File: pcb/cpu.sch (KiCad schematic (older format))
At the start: 34 parts, among them P27 BDM, P57 TX1, P58 RX1, P59 RX0-TX0, P64 CAN-RX-TX, U1 MC9S12XDP512, Y1 16MHz

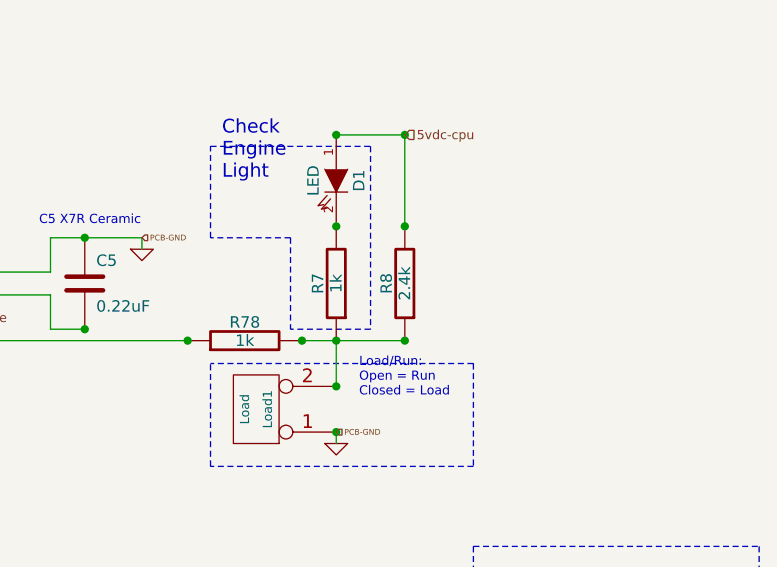
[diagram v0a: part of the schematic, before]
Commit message: Changed 2.4k ohm resistor to 2.43k ohm resistor due to physical size issue.
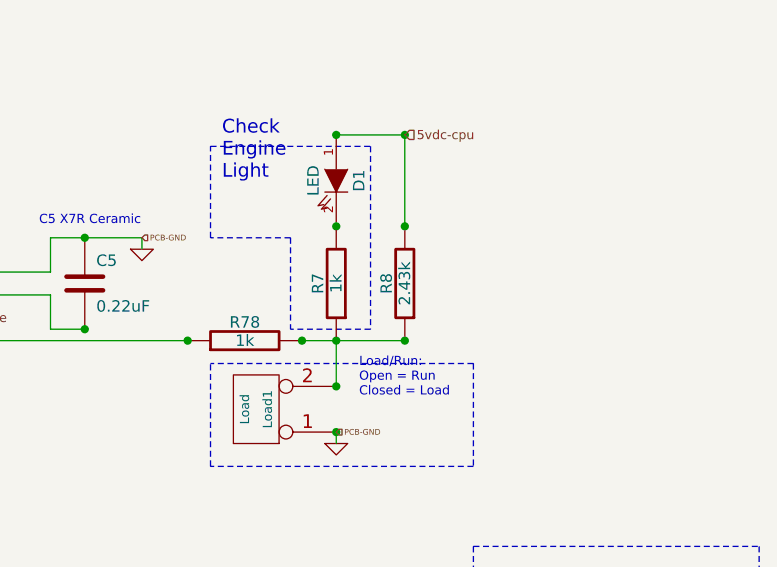
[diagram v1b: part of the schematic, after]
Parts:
- R8: value 2.4k -> 2.43k
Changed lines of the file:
@@
-EESchema Schematic File Version 2  date Wed 18 Sep 2013 09:15:01 PM EDT
+EESchema Schematic File Version 2
 LIBS:opto
 LIBS:power
@@
 LIBS:Jaguar
 LIBS:Jaguar-cache
-EELAYER 24  0
+EELAYER 27 0
 EELAYER END
-$Descr A4 11700 8267
+$Descr A4 11693 8268
+encoding utf-8
 Sheet 2 7
 Title "Jaguar PCB for FreeEMS"
-Date "16 sep 2013"
+Date "7 nov 2013"
 Rev "0.6-alpha"
 Comp "Git: 73f4fbd6d6"
@@
 F 0 "P59" V 5750 800 40  0000 C CNN
 F 1 "RX0-TX0" V 5850 800 40  0000 C CNN
+F 2 "" H 5800 800 60  0001 C CNN
+F 3 "" H 5800 800 60  0001 C CNN
 	1    5800 800
 	0    -1   -1   0
@@
 F 0 "P64" V 4050 1300 40  0000 C CNN
 F 1 "CAN-RX-TX" V 4150 1300 40  0000 C CNN
+F 2 "" H 4100 1300 60  0001 C CNN
+F 3 "" H 4100 1300 60  0001 C CNN
 	1    4100 1300
 	0    -1   -1   0
@@
 F 0 "P57" H 5380 1600 40  0000 L CNN
 F 1 "TX1" H 5300 1655 30  0001 C CNN
+F 2 "" H 5300 1600 60  0001 C CNN
+F 3 "" H 5300 1600 60  0001 C CNN
 	1    5300 1600
 	0    -1   -1   0
@@
 F 0 "P58" H 5480 1600 40  0000 L CNN
 F 1 "RX1" H 5400 1655 30  0001 C CNN
+F 2 "" H 5400 1600 60  0001 C CNN
+F 3 "" H 5400 1600 60  0001 C CNN
 	1    5400 1600
 	0    -1   -1   0
@@
 F 0 "C47" H 3700 400 50  0000 L CNN
 F 1 "10uF" H 3700 250 50  0000 L CNN
+F 2 "" H 3850 550 60  0001 C CNN
+F 3 "" H 3850 550 60  0001 C CNN
 	1    3850 550
 	0    -1   -1   0
@@
 F 0 "R78" V 8630 4850 50  0000 C CNN
 F 1 "1k" V 8550 4850 50  0000 C CNN
+F 2 "" H 8550 4850 60  0001 C CNN
+F 3 "" H 8550 4850 60  0001 C CNN
 	1    8550 4850
 	0    -1   -1   0
@@
 F 0 "PP2" V 3400 1400 50  0000 C CNN
 F 1 "Port P4-7" V 3500 1400 50  0000 C CNN
+F 2 "" H 3450 1400 60  0001 C CNN
+F 3 "" H 3450 1400 60  0001 C CNN
 	1    3450 1400
 	0    -1   -1   0
@@
 F 0 "PP1" V 1800 3000 50  0000 C CNN
 F 1 "Port P0-3" V 1900 3000 50  0000 C CNN
+F 2 "" H 1850 3000 60  0001 C CNN
+F 3 "" H 1850 3000 60  0001 C CNN
 	1    1850 3000
 	-1   0    0    1
@@
 F 0 "C48" H 4650 7650 50  0000 L CNN
 F 1 "10uF" H 4650 7450 50  0000 L CNN
+F 2 "" H 4600 7550 60  0001 C CNN
+F 3 "" H 4600 7550 60  0001 C CNN
 	1    4600 7550
 	0    1    1    0
@@
 F 0 "C5" H 7900 4700 50  0000 L CNN
 F 1 "0.22uF" H 7900 4500 50  0000 L CNN
+F 2 "" H 7850 4600 60  0001 C CNN
+F 3 "" H 7850 4600 60  0001 C CNN
 	1    7850 4600
 	1    0    0    -1
@@
 F 0 "C1" H 1350 4200 50  0000 L CNN
 F 1 "0.22uF" H 1350 4000 50  0000 L CNN
+F 2 "" H 1300 4100 60  0001 C CNN
+F 3 "" H 1300 4100 60  0001 C CNN
 	1    1300 4100
 	-1   0    0    1
@@
 F 0 "Load1" V 8550 5150 40  0000 C CNN
 F 1 "Load" V 8650 5150 40  0000 C CNN
+F 2 "" H 8600 5150 60  0001 C CNN
+F 3 "" H 8600 5150 60  0001 C CNN
 	1    8600 5150
 	-1   0    0    1
@@
 F 0 "#PWR02" H 1300 4350 30  0001 C CNN
 F 1 "GND" H 1300 4280 30  0001 C CNN
+F 2 "" H 1300 4350 60  0001 C CNN
+F 3 "" H 1300 4350 60  0001 C CNN
 	1    1300 4350
 	1    0    0    -1
@@
 F 0 "C44" H 7200 2050 50  0000 L CNN
 F 1 "0.22uF" H 7200 1850 50  0000 L CNN
+F 2 "" H 7150 1950 60  0001 C CNN
+F 3 "" H 7150 1950 60  0001 C CNN
 	1    7150 1950
 	1    0    0    -1
@@
 F 0 "#PWR03" H 5200 6850 30  0001 C CNN
 F 1 "GND" H 5200 6780 30  0001 C CNN
+F 2 "" H 5200 6850 60  0001 C CNN
+F 3 "" H 5200 6850 60  0001 C CNN
 	1    5200 6850
 	1    0    0    -1
@@
 F 0 "#PWR04" H 8450 6000 30  0001 C CNN
 F 1 "GND" H 8450 5930 30  0001 C CNN
+F 2 "" H 8450 6000 60  0001 C CNN
+F 3 "" H 8450 6000 60  0001 C CNN
 	1    8450 6000
 	1    0    0    -1
@@
 F 0 "#PWR05" H 1700 7000 30  0001 C CNN
 F 1 "GND" H 1700 6930 30  0001 C CNN
+F 2 "" H 1700 7000 60  0001 C CNN
+F 3 "" H 1700 7000 60  0001 C CNN
 	1    1700 7000
 	1    0    0    -1
@@
 F 0 "#PWR06" H 1850 7600 30  0001 C CNN
 F 1 "GND" H 1850 7530 30  0001 C CNN
+F 2 "" H 1850 7600 60  0001 C CNN
+F 3 "" H 1850 7600 60  0001 C CNN
 	1    1850 7600
 	1    0    0    -1
@@
 F 0 "#PWR07" H 4300 1100 30  0001 C CNN
 F 1 "GND" H 4300 1030 30  0001 C CNN
+F 2 "" H 4300 1100 60  0001 C CNN
+F 3 "" H 4300 1100 60  0001 C CNN
 	1    4300 1100
 	1    0    0    -1
@@
 F 0 "#PWR08" H 8950 1000 30  0001 C CNN
 F 1 "GND" H 8950 930 30  0001 C CNN
+F 2 "" H 8950 1000 60  0001 C CNN
+F 3 "" H 8950 1000 60  0001 C CNN
 	1    8950 1000
 	1    0    0    -1
@@
 F 0 "#PWR09" H 6100 1850 30  0001 C CNN
 F 1 "GND" H 6100 1780 30  0001 C CNN
+F 2 "" H 6100 1850 60  0001 C CNN
+F 3 "" H 6100 1850 60  0001 C CNN
 	1    6100 1850
 	1    0    0    -1
@@
 F 0 "#PWR010" H 8950 5300 30  0001 C CNN
 F 1 "GND" H 8950 5230 30  0001 C CNN
+F 2 "" H 8950 5300 60  0001 C CNN
+F 3 "" H 8950 5300 60  0001 C CNN
 	1    8950 5300
 	1    0    0    -1
@@
 F 0 "#PWR011" H 8100 4450 30  0001 C CNN
 F 1 "GND" H 8100 4380 30  0001 C CNN
+F 2 "" H 8100 4450 60  0001 C CNN
+F 3 "" H 8100 4450 60  0001 C CNN
 	1    8100 4450
 	1    0    0    -1
@@
 F 0 "#PWR012" H 9950 6850 30  0001 C CNN
 F 1 "GND" H 9950 6780 30  0001 C CNN
+F 2 "" H 9950 6850 60  0001 C CNN
+F 3 "" H 9950 6850 60  0001 C CNN
 	1    9950 6850
 	1    0    0    -1
@@
 F 0 "#PWR013" H 4400 7700 30  0001 C CNN
 F 1 "GND" H 4400 7630 30  0001 C CNN
+F 2 "" H 4400 7700 60  0001 C CNN
+F 3 "" H 4400 7700 60  0001 C CNN
 	1    4400 7700
 	1    0    0    -1
@@
 F 0 "#PWR014" H 4100 7700 30  0001 C CNN
 F 1 "GND" H 4100 7630 30  0001 C CNN
+F 2 "" H 4100 7700 60  0001 C CNN
+F 3 "" H 4100 7700 60  0001 C CNN
 	1    4100 7700
 	1    0    0    -1
@@
 F 0 "D1" H 8950 4250 50  0000 C CNN
 F 1 "LED" H 8950 4050 50  0000 C CNN
+F 2 "" H 8950 4150 60  0001 C CNN
+F 3 "" H 8950 4150 60  0001 C CNN
 	1    8950 4150
 	0    1    1    0
@@
 P 9250 4600
 F 0 "R8" V 9330 4600 50  0000 C CNN
-F 1 "2.4k" V 9250 4600 50  0000 C CNN
+F 1 "2.43k" V 9250 4600 50  0000 C CNN
+F 2 "" H 9250 4600 60  0001 C CNN
+F 3 "" H 9250 4600 60  0001 C CNN
 	1    9250 4600
 	-1   0    0    1
@@
 F 0 "C6" H 1900 7450 50  0000 L CNN
 F 1 "0.1uF" H 1900 7250 50  0000 L CNN
+F 2 "" H 1850 7350 60  0001 C CNN
+F 3 "" H 1850 7350 60  0001 C CNN
 	1    1850 7350
 	1    0    0    -1
@@
 F 1 "MC9S12XDP512" H 4300 3750 50  0000 L BNN
 F 2 "mc9s12xdp512-LQFP112" H 4600 4300 50  0001 C CNN
+F 3 "" H 4600 4150 60  0001 C CNN
 	1    4600 4150
 	1    0    0    -1
@@
 F 0 "P27" H 1200 7450 50  0000 C CNN
 F 1 "BDM" V 1200 7250 40  0000 C CNN
+F 2 "" H 1200 7200 60  0001 C CNN
+F 3 "" H 1200 7200 60  0001 C CNN
 	1    1200 7200
 	1    0    0    -1
@@
 F 0 "R4" V 880 6800 50  0000 C CNN
 F 1 "10k" V 800 6800 50  0000 C CNN
+F 2 "" H 800 6800 60  0001 C CNN
+F 3 "" H 800 6800 60  0001 C CNN
 	1    800  6800
 	-1   0    0    1
@@
 F 0 "R5" V 1930 6800 50  0000 C CNN
 F 1 "10k" V 1850 6800 50  0000 C CNN
+F 2 "" H 1850 6800 60  0001 C CNN
+F 3 "" H 1850 6800 60  0001 C CNN
 	1    1850 6800
 	-1   0    0    1
@@
 F 0 "R1" V 3700 7250 50  0000 C CNN
 F 1 "10k" V 3800 7250 50  0000 C CNN
+F 2 "" H 3800 7250 60  0001 C CNN
+F 3 "" H 3800 7250 60  0001 C CNN
 	1    3800 7250
 	1    0    0    -1
@@
 F 0 "R2" V 3900 7250 50  0000 C CNN
 F 1 "10k" V 4000 7250 50  0000 C CNN
+F 2 "" H 4000 7250 60  0001 C CNN
+F 3 "" H 4000 7250 60  0001 C CNN
 	1    4000 7250
 	1    0    0    -1
@@
 F 0 "R3" V 4100 7250 50  0000 C CNN
 F 1 "10k" V 4200 7250 50  0000 C CNN
+F 2 "" H 4200 7250 60  0001 C CNN
+F 3 "" H 4200 7250 60  0001 C CNN
 	1    4200 7250
 	1    0    0    -1
@@
 F 0 "R7" V 9030 4600 50  0000 C CNN
 F 1 "1k" V 8950 4600 50  0000 C CNN
+F 2 "" H 8950 4600 60  0001 C CNN
+F 3 "" H 8950 4600 60  0001 C CNN
 	1    8950 4600
 	-1   0    0    1
@@
 F 0 "Y1" H 10400 6000 60  0000 C CNN
 F 1 "16MHz" H 10200 5800 60  0000 C CNN
+F 2 "" H 10200 5950 60  0001 C CNN
+F 3 "" H 10200 5950 60  0001 C CNN
 	1    10200 5950
 	1    0    0    -1
@@
 F 0 "C11" H 10500 6700 50  0000 L CNN
 F 1 "20pF" H 10500 6500 50  0000 L CNN
+F 2 "" H 10450 6600 60  0001 C CNN
+F 3 "" H 10450 6600 60  0001 C CNN
 	1    10450 6600
 	-1   0    0    1
@@
 F 0 "C10" H 10000 6700 50  0000 L CNN
 F 1 "20pF" H 10000 6500 50  0000 L CNN
+F 2 "" H 9950 6600 60  0001 C CNN
+F 3 "" H 9950 6600 60  0001 C CNN
 	1    9950 6600
 	-1   0    0    1
@@
 F 0 "R6" V 8230 6750 50  0000 C CNN
 F 1 "3.3k" V 8150 6750 50  0000 C CNN
+F 2 "" H 8150 6750 60  0001 C CNN
+F 3 "" H 8150 6750 60  0001 C CNN
 	1    8150 6750
 	0    -1   -1   0
@@
 F 0 "C9" H 8450 6650 50  0000 L CNN
 F 1 "680pF" H 8450 6450 50  0000 L CNN
+F 2 "" H 8400 6550 60  0001 C CNN
+F 3 "" H 8400 6550 60  0001 C CNN
 	1    8400 6550
 	-1   0    0    1
@@
 F 0 "C7" H 7950 6650 50  0000 L CNN
 F 1 "6.8nF" H 7950 6450 50  0000 L CNN
+F 2 "" H 7900 6550 60  0001 C CNN
+F 3 "" H 7900 6550 60  0001 C CNN
 	1    7900 6550
 	-1   0    0    1
@@
 F 0 "C8" H 8200 6250 50  0000 L CNN
 F 1 "0.22uF" H 8200 6050 50  0000 L CNN
+F 2 "" H 8150 6150 60  0001 C CNN
+F 3 "" H 8150 6150 60  0001 C CNN
 	1    8150 6150
 	1    0    0    -1
@@
 F 0 "C3" H 4650 7400 50  0000 L CNN
 F 1 "0.22uF" H 4650 7200 50  0000 L CNN
+F 2 "" H 4600 7300 60  0001 C CNN
+F 3 "" H 4600 7300 60  0001 C CNN
 	1    4600 7300
 	0    -1   -1   0
@@
 F 0 "C4" H 5950 1650 50  0000 L CNN
 F 1 "0.22uF" H 6050 1550 50  0000 L CNN
+F 2 "" H 5900 1550 60  0001 C CNN
+F 3 "" H 5900 1550 60  0001 C CNN
 	1    5900 1550
 	1    0    0    -1
@@
 F 0 "C2" H 3900 1000 50  0000 L CNN
 F 1 "0.22uF" H 3750 600 50  0000 L CNN
+F 2 "" H 3850 900 60  0001 C CNN
+F 3 "" H 3850 900 60  0001 C CNN
 	1    3850 900
 	0    -1   -1   0

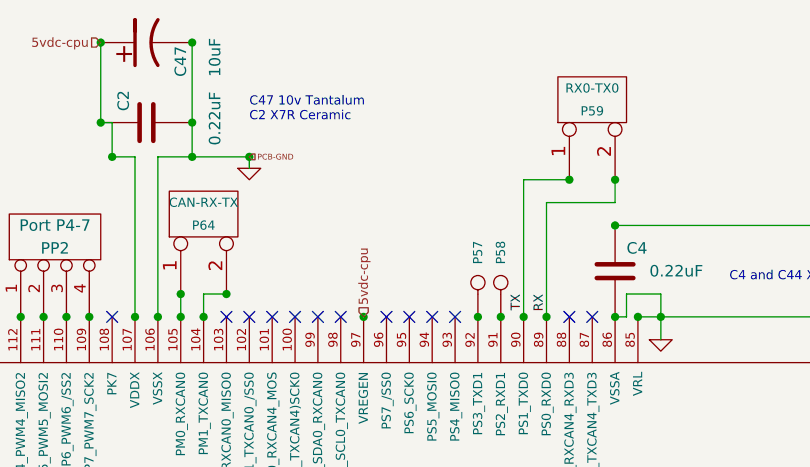
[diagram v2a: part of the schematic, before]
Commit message: Eliminated Pxx designations on the wire connection points and replaced them with the PCB silkscreen designations.
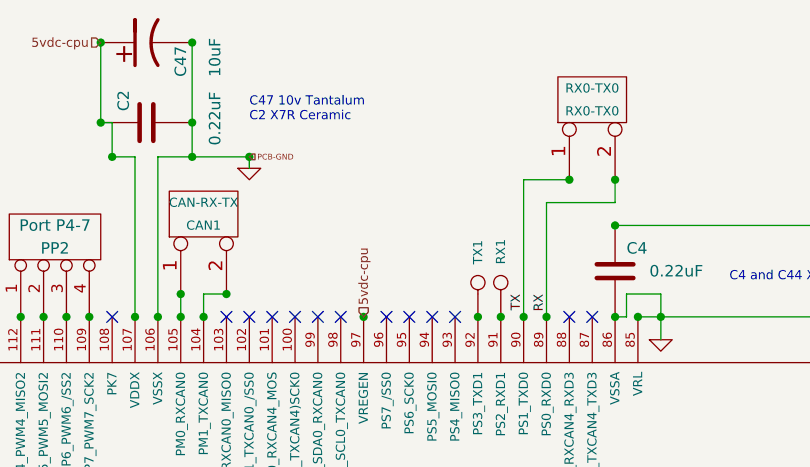
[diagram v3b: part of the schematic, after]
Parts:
- renumbered P64 to CAN1, P59 to RX0-TX0, P58 to RX1, P57 to TX1
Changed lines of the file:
@@
 Sheet 2 7
 Title "Jaguar PCB for FreeEMS"
-Date "17 nov 2013"
+Date "3 dec 2013"
 Rev "0.6-alpha"
 Comp "Git: 73f4fbd6d6"
@@
 	5900 1250 5900 1150
 $Comp
-L CONN_2 P59
+L CONN_2 RX0-TX0
 U 1 1 51A0194D
 P 5800 800
-F 0 "P59" V 5750 800 40  0000 C CNN
+F 0 "RX0-TX0" V 5750 800 40  0000 C CNN
 F 1 "RX0-TX0" V 5850 800 40  0000 C CNN
 F 2 "" H 5800 800 60  0001 C CNN
@@
 $EndComp
 $Comp
-L CONN_2 P64
+L CONN_2 CAN1
 U 1 1 519BDE3D
 P 4100 1300
-F 0 "P64" V 4050 1300 40  0000 C CNN
+F 0 "CAN1" V 4050 1300 40  0000 C CNN
 F 1 "CAN-RX-TX" V 4150 1300 40  0000 C CNN
 F 2 "" H 4100 1300 60  0001 C CNN
@@
 Fan-PK4
 $Comp
-L CONN_1 P57
+L CONN_1 TX1
 U 1 1 505D24DB
 P 5300 1600
-F 0 "P57" H 5380 1600 40  0000 L CNN
+F 0 "TX1" H 5380 1600 40  0000 L CNN
 F 1 "TX1" H 5300 1655 30  0001 C CNN
 F 2 "" H 5300 1600 60  0001 C CNN
@@
 $EndComp
 $Comp
-L CONN_1 P58
+L CONN_1 RX1
 U 1 1 505D24CE
 P 5400 1600
-F 0 "P58" H 5480 1600 40  0000 L CNN
+F 0 "RX1" H 5480 1600 40  0000 L CNN
 F 1 "RX1" H 5400 1655 30  0001 C CNN
 F 2 "" H 5400 1600 60  0001 C CNN

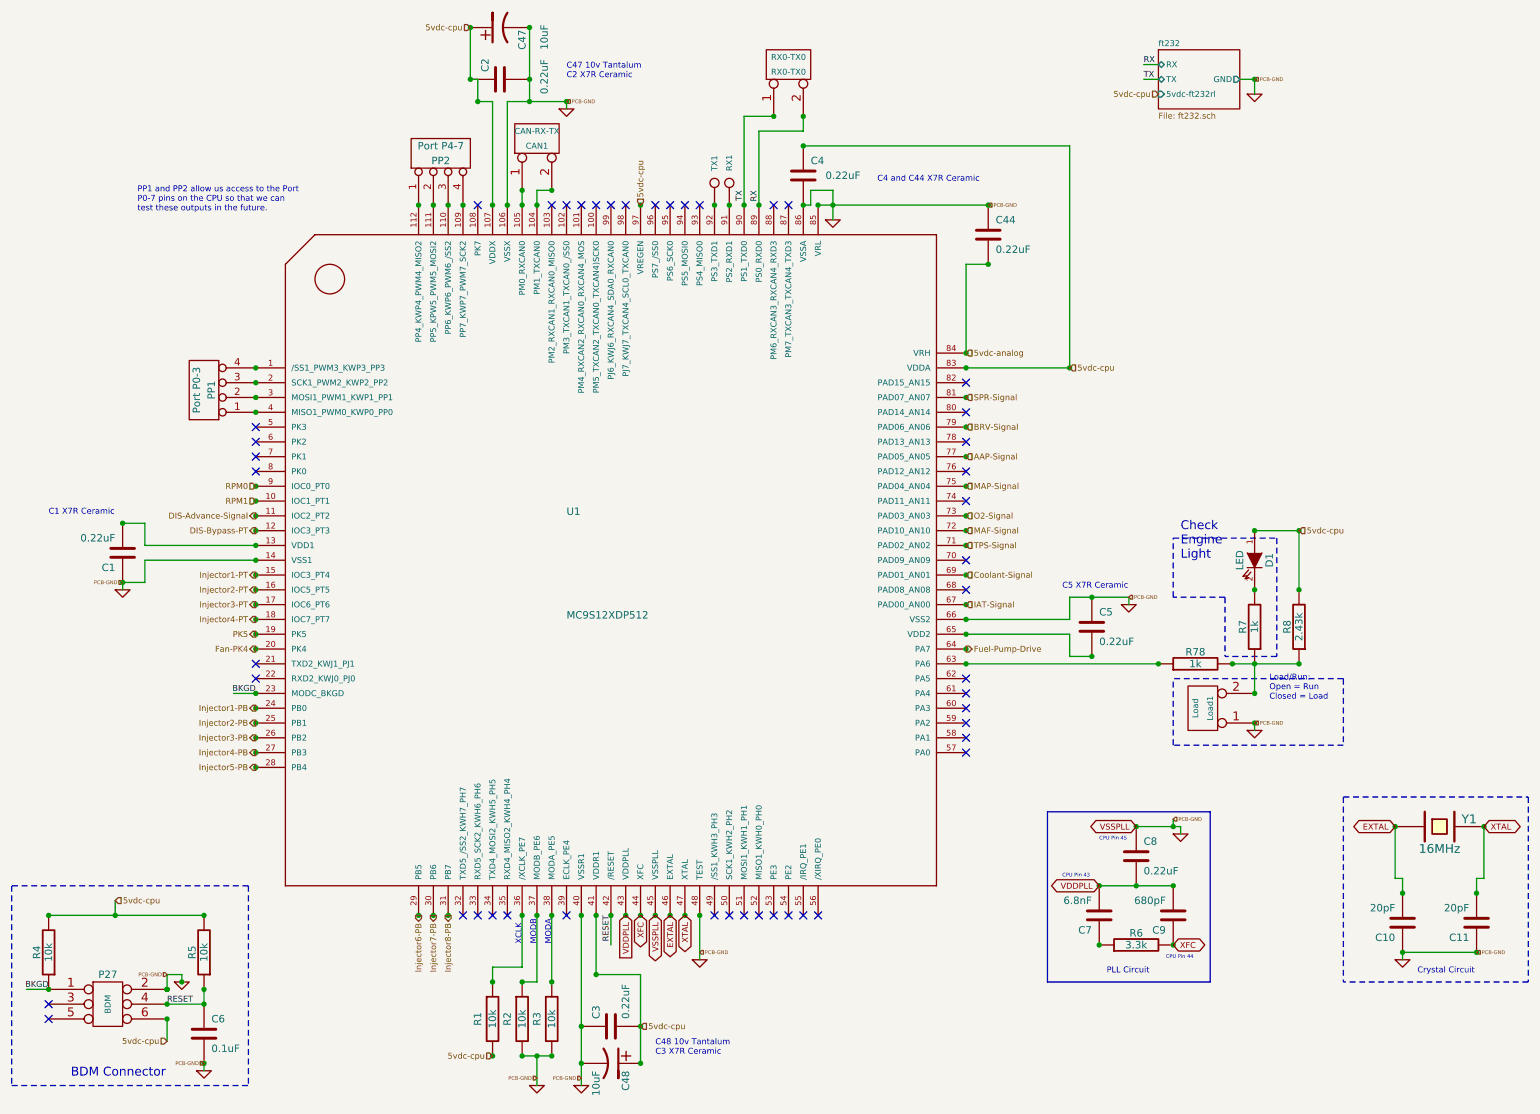
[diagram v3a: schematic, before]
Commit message: Added LEDs and resistors to ignitor outputs.
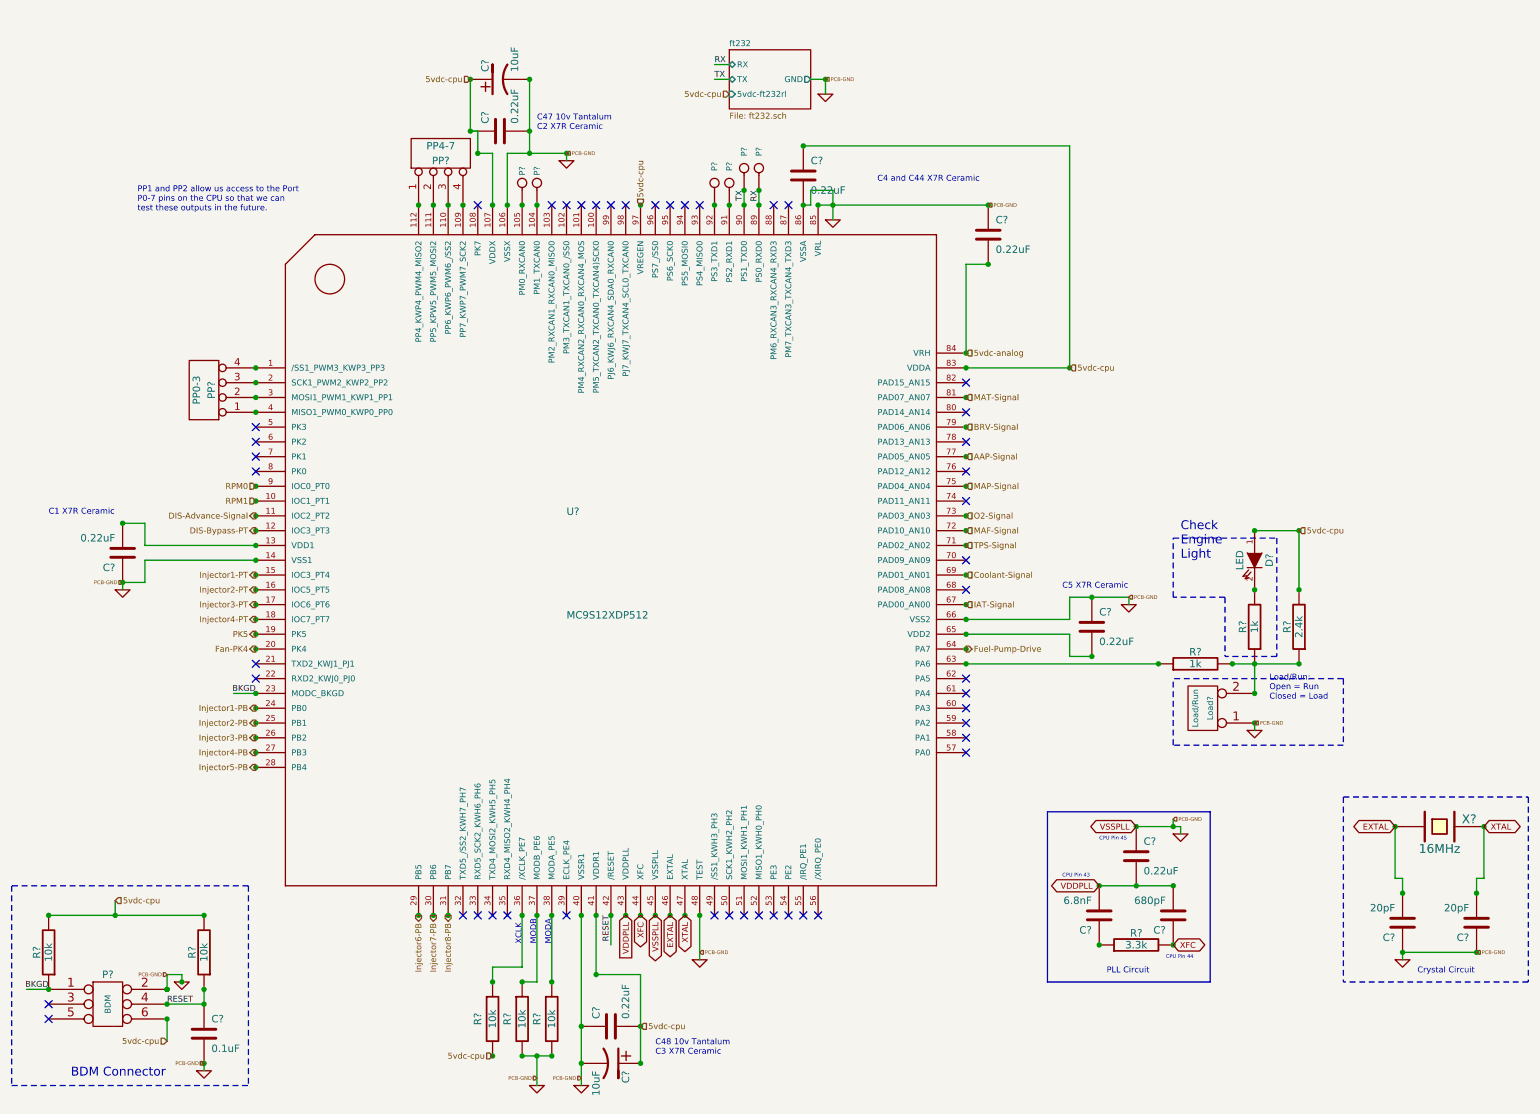
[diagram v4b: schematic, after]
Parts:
- removed CAN1: CAN-RX-TX, symbol CONN_2
- removed RX0-TX0: RX0-TX0, symbol CONN_2
- added P?: TX, symbol CONN_1
- added P?: RX, symbol CONN_1
- added P?: RXCAN0, symbol CONN_1
- added P?: TXCAN0, symbol CONN_1
- Load?: renamed from Load1; value Load -> Load/Run
- PP?: renamed from PP1; value Port P0-3 -> PP0-3
- PP?: renamed from PP2; value Port P4-7 -> PP4-7
- R?: renamed from R8; value 2.43k -> 2.4k
- renumbered C2 to C?, C4 to C?, C3 to C?, C8 to C?, C7 to C?, C9 to C?, C10 to C?, C11 to C?, C6 to C?, C44 to C?, C1 to C?, C5 to C?, C48 to C?, C47 to C?, D1 to D?, P27 to P?, RX1 to P?, TX1 to P?, R6 to R?, R7 to R?, R3 to R?, R2 to R?, R1 to R?, R5 to R?, R4 to R?, R78 to R?, U1 to U?, Y1 to X?
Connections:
- net labels added: MAT-Signal
- net labels removed: SPR-Signal
- wire segments 88 -> 82
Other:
- moved on the sheet: C?
